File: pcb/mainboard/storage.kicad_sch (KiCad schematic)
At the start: 5 parts, among them J401 MICRO_SD(TFC-WPAPR-08)

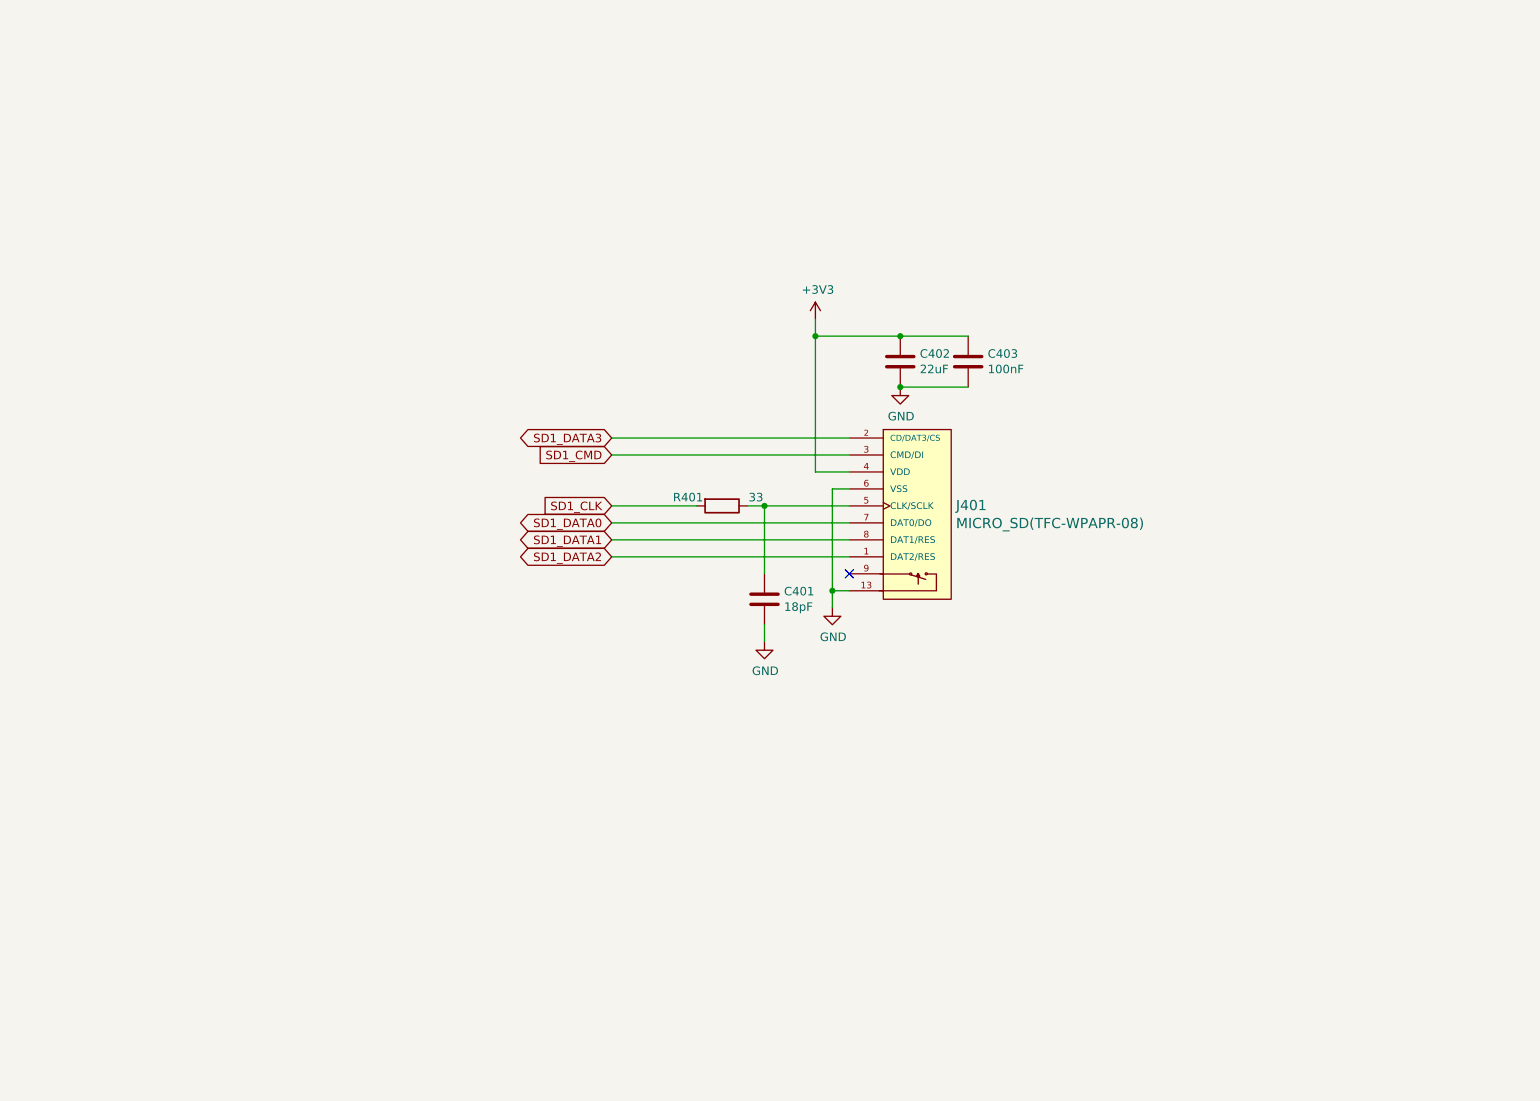
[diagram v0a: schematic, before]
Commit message: pcb: preliminary r0p1 schematics
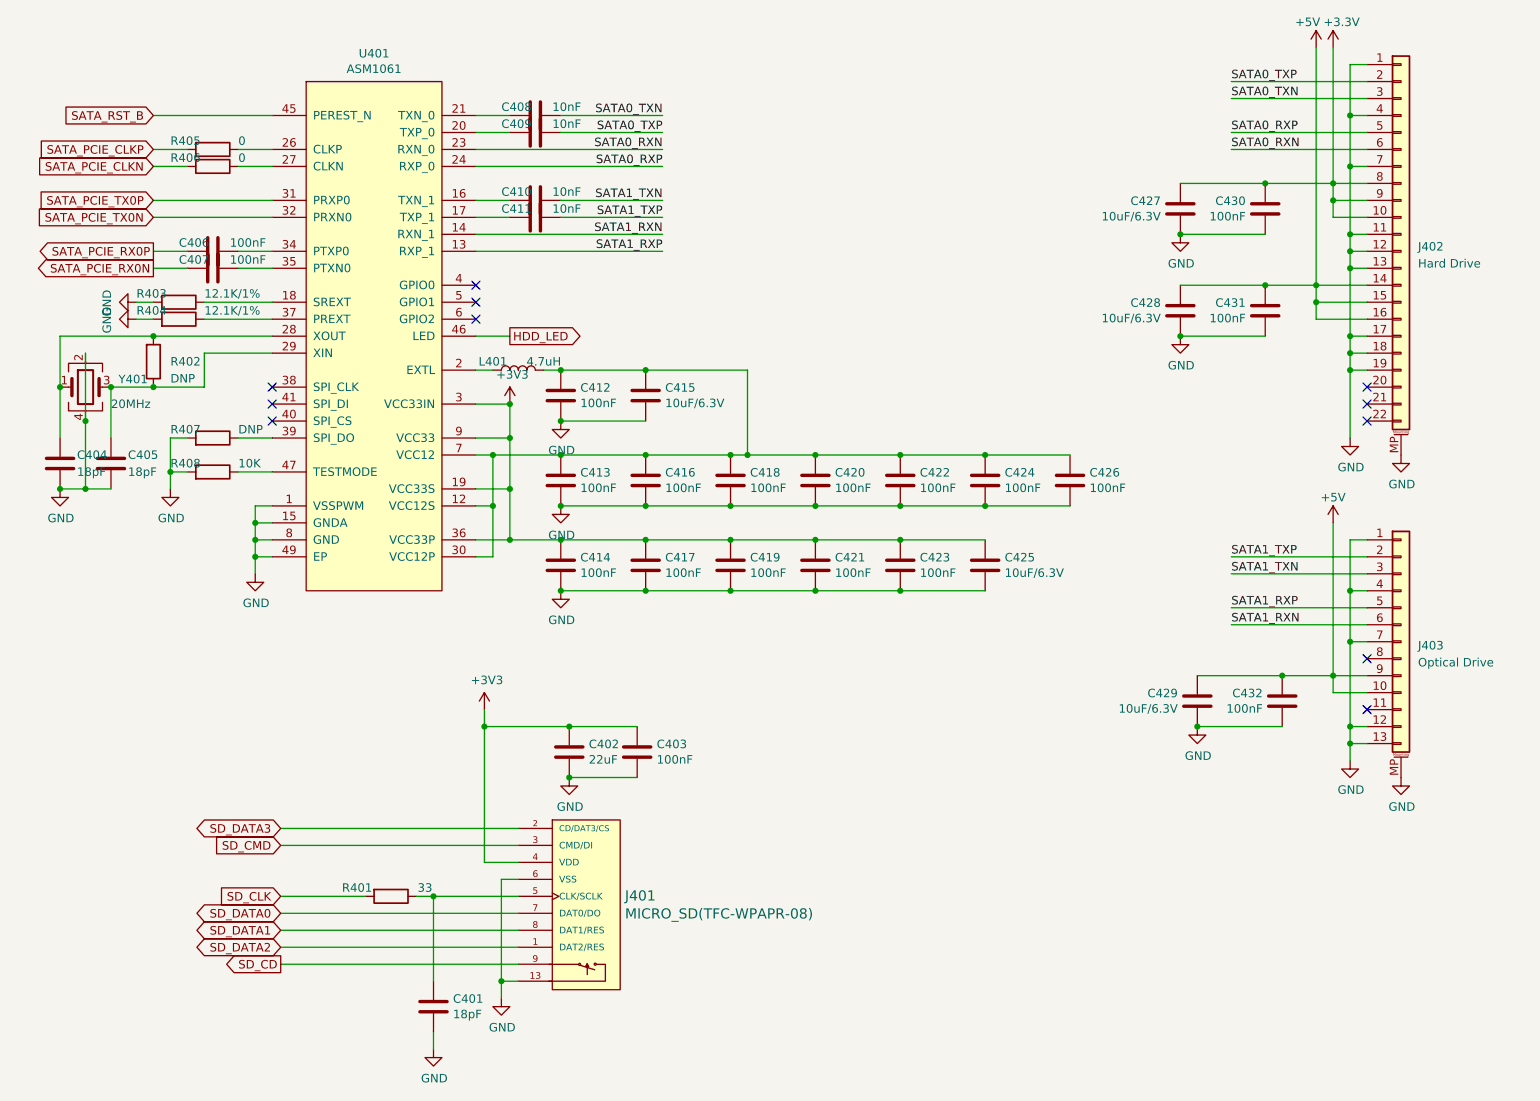
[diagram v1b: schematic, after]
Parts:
- added C404, C405: 18pF, Capacitor_SMD:C_0603_1608Metric, symbol Device:C
- added C406, C407: 100nF, Capacitor_SMD:C_0603_1608Metric, symbol Device:C
- added C408, C409, C410, C411: 10nF, Capacitor_SMD:C_0603_1608Metric, symbol Device:C
- added C412, C413, C414, C416, C417, C418, C419, C420, C421, C422, C423, C424, C426, C430, C431, C432: 100nF, symbol Device:C
- added C415, C425, C427, C428, C429: 10uF/6.3V, symbol Device:C
- added J402: Hard Drive, footprints:TE_2023246-2, symbol Connector_Generic_MountingPin:Conn_01x22_MountingPin
- added J403: Optical Drive, footprints:TE_1735413-1, symbol Connector_Generic_MountingPin:Conn_01x13_MountingPin
- added L401: 4.7uH, symbol Device:L
- added R402, R407: DNP, Resistor_SMD:R_0603_1608Metric, symbol Device:R
- added R403, R404: 12.1K/1%, Resistor_SMD:R_0603_1608Metric, symbol Device:R
- added R405, R406: 0, Resistor_SMD:R_0603_1608Metric, symbol Device:R
- added R408: 10K, Resistor_SMD:R_0603_1608Metric, symbol Device:R
- added U401: ASM1061, Package_DFN_QFN:QFN-48-1EP_7x7mm_P0.5mm_EP5.15x5.15mm_ThermalVias, symbol symbols:ASM1061
- added Y401: 20MHz, Crystal:Crystal_SMD_3225-4Pin_3.2x2.5mm, symbol Device:Crystal_GND24
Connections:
- net +3V3: now also C414.1, C417.1, C419.1, C421.1, C423.1, C425.1, C427.1, C430.1, J402.10 (Pin_10), J402.8 (Pin_8), J402.9 (Pin_9), U401.19 (VCC33S), U401.3 (VCC33IN), U401.36 (VCC33P), U401.44 (VCC33), U401.9 (VCC33)
- net GND: now also C404.1, C405.1, C412.2, C413.2, C414.2, C415.2, C416.2, C417.2, C418.2, C419.2, C420.2, C421.2, C422.2, C423.2, C424.2, C425.2, C426.2, C427.2, C428.2, C429.2, C430.2, C431.2, C432.2, J402.1 (Pin_1), J402.11 (Pin_11), J402.12 (Pin_12), J402.13 (Pin_13), J402.17 (Pin_17), J402.18 (Pin_18), J402.19 (Pin_19), J402.4 (Pin_4), J402.7 (Pin_7), J402.MP (MountPin), J403.1 (Pin_1), J403.12 (Pin_12), J403.13 (Pin_13), J403.4 (Pin_4), J403.7 (Pin_7), J403.MP (MountPin), R403.2, R404.2, R407.2, R408.2, U401.1 (VSSPWM), U401.10 (GND), U401.15 (GNDA), U401.22 (GNDA), U401.33 (GNDA), U401.42 (GND), U401.49 (EP), U401.8 (GND), Y401.2, Y401.4
- net SD_CD: now reaches J401.9
- net SD1_CLK renamed SD_CLK
- net SD1_CMD renamed SD_CMD
- net SD1_DATA0 renamed SD_DATA0
- net SD1_DATA1 renamed SD_DATA1
- net SD1_DATA2 renamed SD_DATA2
- net SD1_DATA3 renamed SD_DATA3
- new net: C404.2, R402.2, U401.28 (XOUT), Y401.1
- new net: C405.2, R402.1, U401.29 (XIN), Y401.3
- new net: R404.1, U401.37 (PREXT)
- new net: R407.1, U401.39 (SPI_DO)
- new net: C406.1, U401.34 (PTXP0)
- new net: R406.1, U401.27 (CLKN)
- new net: R408.1, U401.47 (TESTMODE)
- new net: C410.2, U401.16 (TXN_1)
- new net: C411.2, U401.17 (TXP_1)
- new net: L401.1, U401.2 (EXTL)
- new net: R403.1, U401.18 (SREXT)
- new net: R405.1, U401.26 (CLKP)
- new net: C409.2, U401.20 (TXP_0)
- new net: C408.2, U401.21 (TXN_0)
- new net: C407.1, U401.35 (PTXN0)
- new net +5V: C428.1, C429.1, C431.1, C432.1, J402.14 (Pin_14), J402.15 (Pin_15), J402.16 (Pin_16), J403.10 (Pin_10), J403.9 (Pin_9)
- new net HDD_LED: U401.46 (LED)
- new net SATA0_RXN: J402.6 (Pin_6), U401.23 (RXN_0)
- new net SATA0_RXP: J402.5 (Pin_5), U401.24 (RXP_0)
- new net SATA0_TXN: C408.1, J402.3 (Pin_3)
- new net SATA0_TXP: C409.1, J402.2 (Pin_2)
- new net SATA1_RXN: J403.6 (Pin_6), U401.14 (RXN_1)
- new net SATA1_RXP: J403.5 (Pin_5), U401.13 (RXP_1)
- new net SATA1_TXN: C410.1, J403.3 (Pin_3)
- new net SATA1_TXP: C411.1, J403.2 (Pin_2)
- new net SATA_PCIE_CLKN: R406.2
- new net SATA_PCIE_CLKP: R405.2
- new net SATA_PCIE_RX0N: C407.2
- new net SATA_PCIE_RX0P: C406.2
- new net SATA_PCIE_TX0N: U401.32 (PRXN0)
- new net SATA_PCIE_TX0P: U401.31 (PRXP0)
- new net SATA_RST_B: U401.45 (PEREST_N)
- new net VCC12: C412.1, C413.1, C415.1, C416.1, C418.1, C420.1, C422.1, C424.1, C426.1, L401.2, U401.11 (VCC12), U401.12 (VCC12S), U401.25 (VCC12S), U401.30 (VCC12P), U401.43 (VCC12), U401.48 (VCC12), U401.7 (VCC12)
- no-connect marks 1 -> 11
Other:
- company: Copyright EI-2030 2021. / Engineer: Wenting Zhang -> Copyright Modos 2021. / Engineer: Wenting Zhang
- moved on the sheet: C401, C402, C403, J401, R401

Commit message: pcb: initial placement for mb
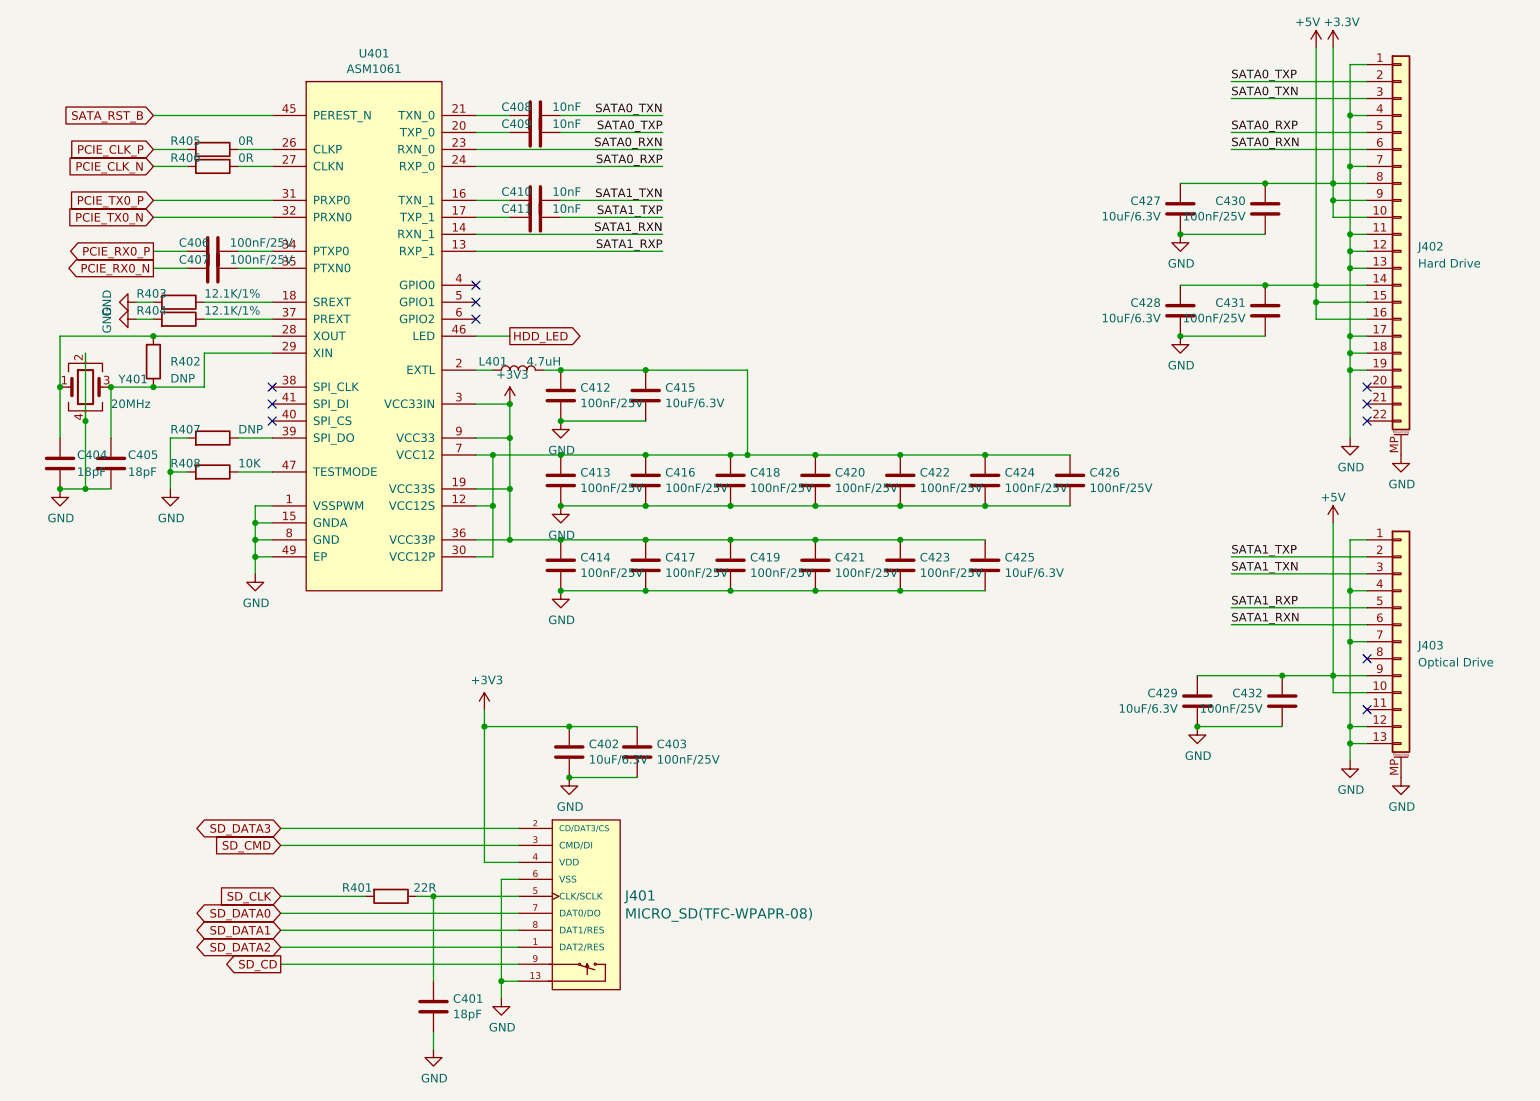
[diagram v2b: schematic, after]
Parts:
- C401: LCSC (none) -> C182481; Ref.Price (none) -> 0.0061
- C402: value 22uF -> 10uF/6.3V; LCSC (none) -> C105490; Ref.Price (none) -> 0.0165
- C403: value 100nF -> 100nF/25V; LCSC (none) -> C56392; Ref.Price (none) -> 0.0023
- C404, C405: footprint Capacitor_SMD:C_0603_1608Metric -> Capacitor_SMD:C_0402_1005Metric; LCSC (none) -> C182481; Ref.Price (none) -> 0.0061
- C406, C407: value 100nF -> 100nF/25V; footprint Capacitor_SMD:C_0603_1608Metric -> Capacitor_SMD:C_0402_1005Metric; LCSC (none) -> C56392; Ref.Price (none) -> 0.0023
- C408, C409, C410, C411: footprint Capacitor_SMD:C_0603_1608Metric -> Capacitor_SMD:C_0402_1005Metric; LCSC (none) -> C1524; Ref.Price (none) -> 0.0013
- C412, C413, C414, C416, C417, C418, C419, C420, C421, C422, C423, C424, C426, C430, C431, C432: value 100nF -> 100nF/25V; footprint (none) -> Capacitor_SMD:C_0402_1005Metric; LCSC (none) -> C56392; Ref.Price (none) -> 0.0023
- C415, C425, C427, C428, C429: footprint (none) -> Capacitor_SMD:C_0603_1608Metric; LCSC (none) -> C105490; Ref.Price (none) -> 0.0165
- J401: LCSC (none) -> C508700; Ref.Price (none) -> 0.651
- J402: LCSC (none) -> A119693-ND; Ref.Price (none) -> 2.408
- J403: LCSC (none) -> A117820CT-ND; Ref.Price (none) -> 1.671
- L401: footprint (none) -> footprints:L_1212; LCSC (none) -> C340379; Ref.Price (none) -> 0.0643
- R401: value 33 -> 22R; LCSC (none) -> C93929; Ref.Price (none) -> 0.002
- R402, R407: footprint Resistor_SMD:R_0603_1608Metric -> Resistor_SMD:R_0402_1005Metric; LCSC (none) -> -; Ref.Price (none) -> 0
- R403, R404: footprint Resistor_SMD:R_0603_1608Metric -> Resistor_SMD:R_0402_1005Metric; LCSC (none) -> C132157; Ref.Price (none) -> 0.0008
- R405, R406: value 0 -> 0R; footprint Resistor_SMD:R_0603_1608Metric -> Resistor_SMD:R_0402_1005Metric; LCSC (none) -> C60485; Ref.Price (none) -> 0.0008
- R408: footprint Resistor_SMD:R_0603_1608Metric -> Resistor_SMD:R_0402_1005Metric; LCSC (none) -> C60489; Ref.Price (none) -> 0.0006
- U401: Ref.Price (none) -> 4.21
- Y401: LCSC (none) -> C555600; Ref.Price (none) -> 0.1011
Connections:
- net SATA_PCIE_CLKN renamed PCIE_CLK_N
- net SATA_PCIE_CLKP renamed PCIE_CLK_P
- net SATA_PCIE_RX0N renamed PCIE_RX0_N
- net SATA_PCIE_RX0P renamed PCIE_RX0_P
- net SATA_PCIE_TX0N renamed PCIE_TX0_N
- net SATA_PCIE_TX0P renamed PCIE_TX0_P

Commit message: pcb: r0.1 mb routing done
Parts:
- removed C401, C404, C405: 18pF, Capacitor_SMD:C_0402_1005Metric, symbol Device:C
- removed C402, C415, C425, C427, C428, C429: 10uF/6.3V, Capacitor_SMD:C_0603_1608Metric, symbol Device:C
- removed C403, C406, C407, C412, C413, C414, C416, C417, C418, C419, C420, C421, C422, C423, C424, C426, C430, C431, C432: 100nF/25V, Capacitor_SMD:C_0402_1005Metric, symbol Device:C
- removed C408, C409, C410, C411: 10nF, Capacitor_SMD:C_0402_1005Metric, symbol Device:C
- removed J401: MICRO_SD(TFC-WPAPR-08), footprints:TFC-WPAPR-08, symbol symbols:MICRO_SD(TFC-WPAPR-08)
- removed J402: Hard Drive, footprints:TE_2023246-2, symbol Connector_Generic_MountingPin:Conn_01x22_MountingPin
- removed J403: Optical Drive, footprints:TE_1735413-1, symbol Connector_Generic_MountingPin:Conn_01x13_MountingPin
- removed L401: 4.7uH, footprints:L_1212, symbol Device:L
- removed R401: 22R, Resistor_SMD:R_0402_1005Metric, symbol Device:R
- removed R402, R407: DNP, Resistor_SMD:R_0402_1005Metric, symbol Device:R
- removed R403, R404: 12.1K/1%, Resistor_SMD:R_0402_1005Metric, symbol Device:R
- removed R405, R406: 0R, Resistor_SMD:R_0402_1005Metric, symbol Device:R
- removed R408: 10K, Resistor_SMD:R_0402_1005Metric, symbol Device:R
- removed U401: ASM1061, Package_DFN_QFN:QFN-48-1EP_7x7mm_P0.5mm_EP5.15x5.15mm_ThermalVias, symbol symbols:ASM1061
- removed Y401: 20MHz, Crystal:Crystal_SMD_3225-4Pin_3.2x2.5mm, symbol Device:Crystal_GND24
- added C615, C617, C621, C625: 100nF/25V, Capacitor_SMD:C_0402_1005Metric, symbol Device:C
- added C623: 10uF/6.3V, Capacitor_SMD:C_0603_1608Metric, symbol Device:C
- added C627: 1uF, Capacitor_SMD:C_0402_1005Metric, symbol Device:C
- added J602: Bus_M.2_Socket_M, footprints:M2_MKEY, symbol Connector:Bus_M.2_Socket_M
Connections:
- net +3V3: now also C615.1, C617.1, C621.1, C623.1, C625.1, C627.1, J602.12 (3.3V), J602.14 (3.3V), J602.16 (3.3V), J602.18 (3.3V), J602.2 (3.3V), J602.4 (3.3V), J602.70 (3.3V), J602.72 (3.3V), J602.74 (3.3V)
- net GND: now also C615.2, C617.2, C621.2, C623.2, C625.2, C627.2, J602.1 (GND), J602.15 (GND), J602.21 (GND), J602.27 (GND), J602.3 (GND), J602.33 (GND), J602.39 (GND), J602.45 (GND), J602.51 (GND), J602.57 (GND), J602.71 (GND), J602.73 (GND), J602.75 (GND), J602.9 (GND)
- net HDD_LED: now also J602.10 (DAS/~{DSS}/~{LED1})
- net PCIE_CLK_N: now also J602.53 (REFCLKn)
- net PCIE_CLK_P: now also J602.55 (REFCLKp)
- net PCIE_RX0_N: now also J602.41 (PERn0/SATA-B+)
- net PCIE_RX0_P: now also J602.43 (PERp0/SATA-B-)
- net PCIE_TX0_N: now also J602.47 (PETn0/SATA-A-)
- net PCIE_TX0_P: now also J602.49 (PETp0/SATA-A+)
- new net PCIE_PERST: J602.50 (~{PERST})
- no-connect marks 11 -> 17
